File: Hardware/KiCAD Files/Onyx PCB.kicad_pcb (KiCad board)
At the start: 2 copper layers, 105.2 x 71.1 mm, 104 parts, among them J1 X Axis, J10 servo pins, J11 Conn_01x03_Male, J12 Screw_Terminal_01x02, J13 5V_Terminal, J14 3.3V_Terminal, J2 Y Axis, J3 Z Axis, J4 USB_B_Micro, J5 A Axis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

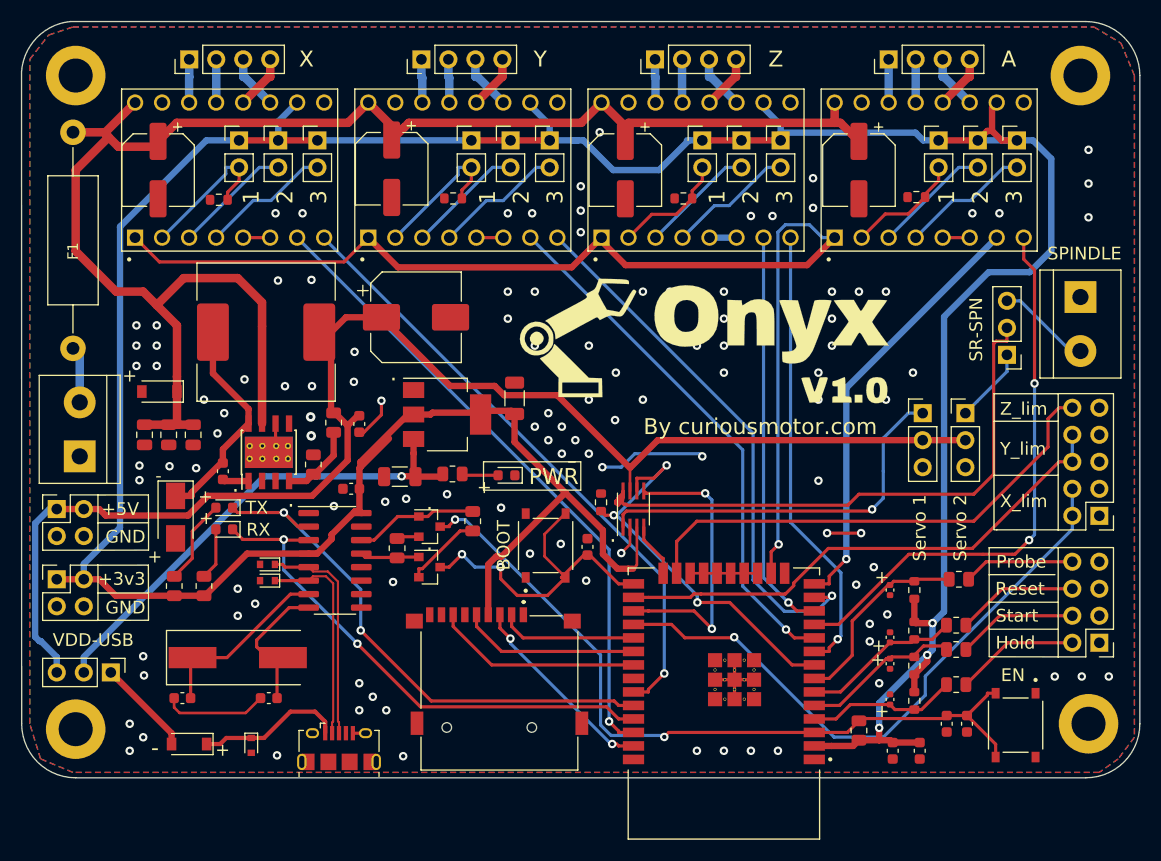
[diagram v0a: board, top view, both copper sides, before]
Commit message: Changed individual MS-config jumpers to blocks for easier soldering
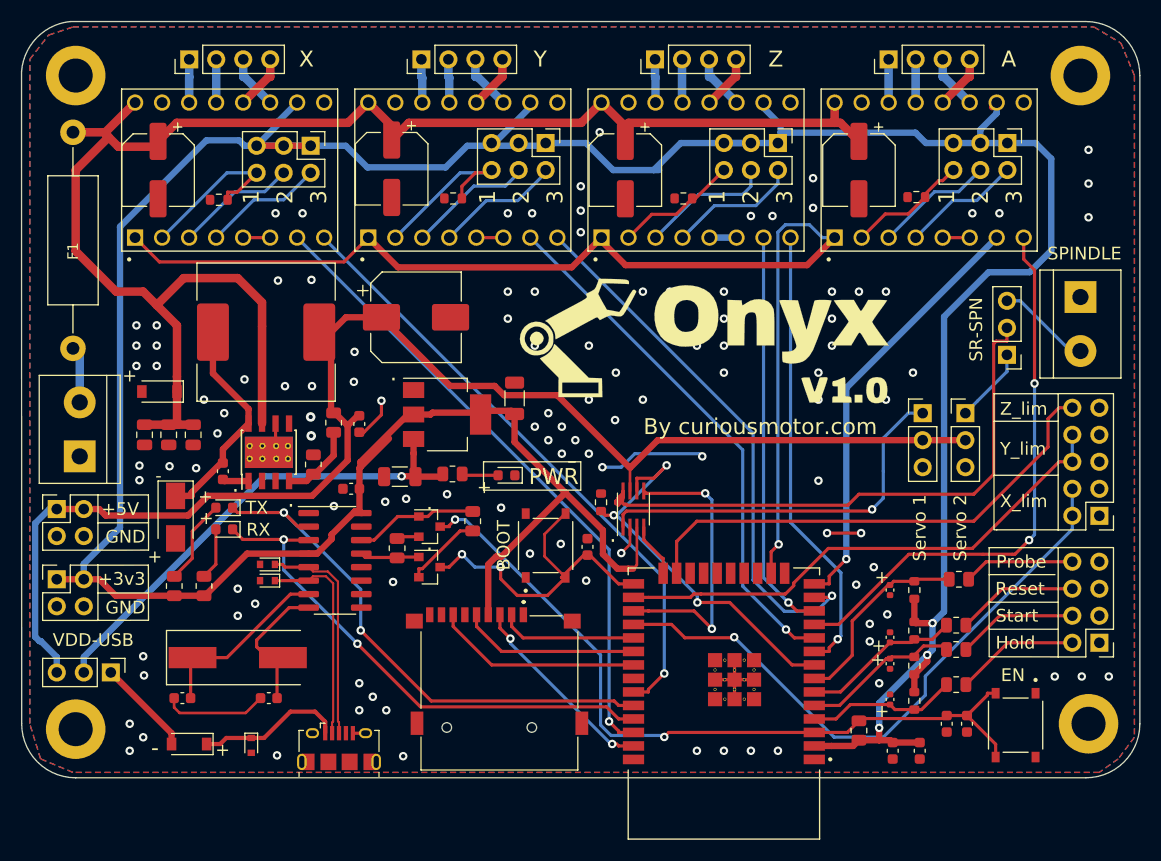
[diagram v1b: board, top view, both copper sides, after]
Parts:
- removed JP1, JP10, JP11, JP12, JP2, JP3, JP4, JP5, JP6, JP7, JP8, JP9: Jumper_NO_Small, Connector_PinHeader_2.54mm:PinHeader_1x02_P2.54mm_Vertical
- added J15: MS_Jumpers, Connector_PinHeader_2.54mm:PinHeader_2x03_P2.54mm_Vertical, F.Cu at (138.9, 87.9)
- added J16: MS_Jumpers, Connector_PinHeader_2.54mm:PinHeader_2x03_P2.54mm_Vertical, F.Cu at (161.0, 87.6)
- added J17: MS_Jumpers, Connector_PinHeader_2.54mm:PinHeader_2x03_P2.54mm_Vertical, F.Cu at (182.9, 87.6)
- added J18: MS_Jumpers, Connector_PinHeader_2.54mm:PinHeader_2x03_P2.54mm_Vertical, F.Cu at (204.5, 87.6)
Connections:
- H1 pad 1: Net-(H1-Pad1) -> unconnected-(H1-Pad1)
- H2 pad 1: Net-(H2-Pad1) -> unconnected-(H2-Pad1)
- H3 pad 1: Net-(H3-Pad1) -> unconnected-(H3-Pad1)
- H4 pad 1: Net-(H4-Pad1) -> unconnected-(H4-Pad1)
- J4 pad 4: Net-(J4-Pad4) -> unconnected-(J4-Pad4)
- J7 pad 1: Net-(J7-Pad1) -> unconnected-(J7-Pad1)
- J7 pad 8: Net-(J7-Pad8) -> unconnected-(J7-Pad8)
- J7 pad 9: Net-(J7-Pad9) -> unconnected-(J7-Pad9)
- J7 pad MP1: Net-(J7-PadMP1) -> unconnected-(J7-PadMP1)
- J7 pad MP2: Net-(J7-PadMP2) -> unconnected-(J7-PadMP2)
- J7 pad MP3: Net-(J7-PadMP3) -> unconnected-(J7-PadMP3)
- J7 pad MP4: Net-(J7-PadMP4) -> unconnected-(J7-PadMP4)
- U2 pad 17: Net-(U2-Pad17) -> unconnected-(U2-Pad17)
- U2 pad 18: Net-(U2-Pad17) -> unconnected-(U2-Pad18)
- U2 pad 19: Net-(U2-Pad17) -> unconnected-(U2-Pad19)
- U2 pad 20: Net-(U2-Pad17) -> unconnected-(U2-Pad20)
- U2 pad 21: Net-(U2-Pad17) -> unconnected-(U2-Pad21)
- U2 pad 22: Net-(U2-Pad17) -> unconnected-(U2-Pad22)
- U2 pad 32: Net-(U2-Pad32) -> unconnected-(U2-Pad32)
- U5 pad 10: Net-(U5-Pad10) -> unconnected-(U5-Pad10)
- U5 pad 11: Net-(U5-Pad11) -> unconnected-(U5-Pad11)
- U5 pad 12: Net-(U5-Pad12) -> unconnected-(U5-Pad12)
- U5 pad 15: Net-(U5-Pad15) -> unconnected-(U5-Pad15)
- U5 pad 9: Net-(U5-Pad9) -> unconnected-(U5-Pad9)
- U7 pad 2: Net-(U7-Pad2) -> unconnected-(U7-Pad2)
- U7 pad 3: Net-(U7-Pad3) -> unconnected-(U7-Pad3)
- U7 pad 5: Net-(U7-Pad5) -> unconnected-(U7-Pad5)
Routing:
- net +3V3: track 328.5 -> 337.1 mm
- net Net-(U2-Pad17): track 6.35 -> 0.00 mm
- net Net-(J16-Pad6): track 13.6 -> 16.0 mm
- net Net-(J15-Pad6): track 13.8 -> 15.6 mm
- net Net-(J17-Pad4): track 10.8 -> 12.5 mm
- net Net-(J18-Pad2): track 12.3 -> 11.3 mm
- net Net-(J15-Pad2): track 12.3 -> 11.4 mm
- net Net-(J17-Pad6): track 10.8 -> 11.6 mm
- net Net-(J16-Pad2): track 12.2 -> 11.6 mm
- net Net-(J16-Pad4): track 11.0 -> 11.6 mm
- net Net-(J18-Pad6): track 10.9 -> 11.4 mm
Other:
- net class 3v3 Line removed
- net class 5v line removed
- net class Default removed
- net class High Power removed
- net class MidSize removed
